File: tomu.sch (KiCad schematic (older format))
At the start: 15 parts, among them P1 USART0, P2 DEBUG, P3 USB-PCB, U1 EFM32HG309

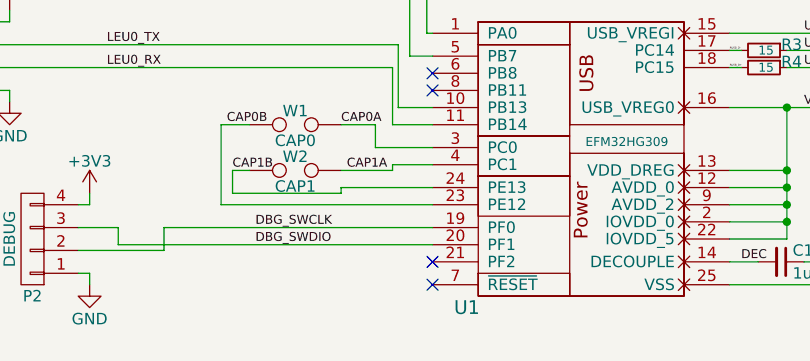
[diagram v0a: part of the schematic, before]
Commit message: Making pin 21 gnd.
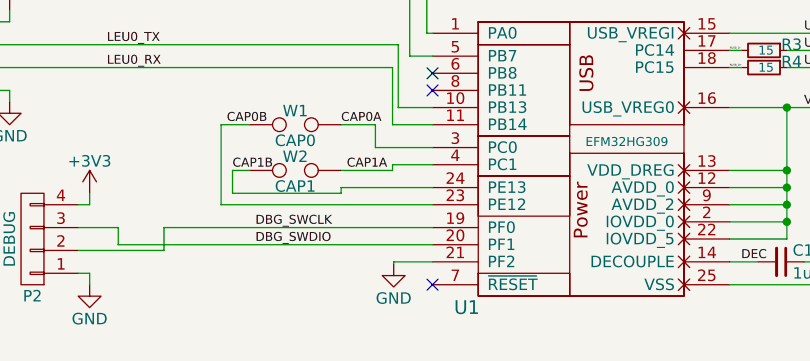
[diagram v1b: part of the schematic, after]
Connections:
- net GND: now also U1.21 (PF2)
- no-connect marks 4 -> 3
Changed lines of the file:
@@
 PB8 - US0_RX\nPB7 - US0_TX\n\nPA0 - Timer 0 Capture Compare Channel 0 -- For PWM - LED0 \nPB7 - Timer 1 Capture Compare Channel 0 -- For PWM - LED1\n\nPC0 - ACMP0_CH0 - Capacitive Touch 0\nPC1 - ACMP0_CH1 - Capacitive Touch 1\n\nPC14 - USB_DM\nPC15 - USB_DP\n\nPE12 - ADC0_CH0\nPE13 - ADC0_CH1\n\nPF0 - DBG_SWCLK #0 - BOOT_RX\nPF1 - DBG_SWDIO #0 - BOOT_TX\n\n
 NoConn ~ 4200 4125
-NoConn ~ 4200 4025
 Text Label 3800 3425 0    39   ~ 0
 CAP0A
@@
 NoConn ~ 4200 3200
 NoConn ~ 4200 3275
+$Comp
+L GND #PWR?
+U 1 1 57A1602A
+P 4030 4035
+F 0 "#PWR?" H 4030 3785 50  0001 C CNN
+F 1 "GND" H 4030 3885 50  0000 C CNN
+F 2 "" H 4030 4035 50  0000 C CNN
+F 3 "" H 4030 4035 50  0000 C CNN
+	1    4030 4035
+	1    0    0    -1
+$EndComp
+Wire Wire Line
+	4200 4025 4030 4025
+Wire Wire Line
+	4030 4025 4030 4035
 $EndSCHEMATC

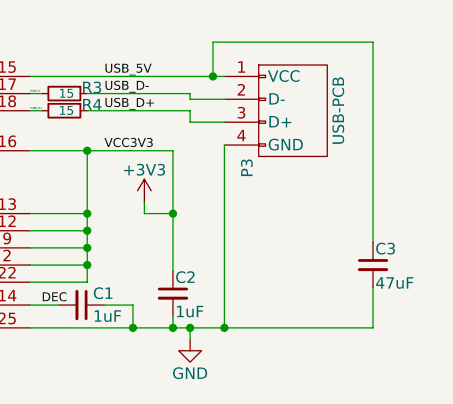
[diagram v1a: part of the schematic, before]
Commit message: 4.7uF not 47uF
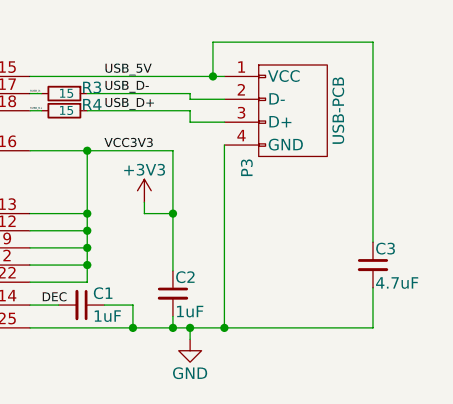
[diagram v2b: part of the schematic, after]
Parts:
- C3: value 47uF -> 4.7uF
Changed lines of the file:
@@
 P 7000 3850
 F 0 "C3" H 7010 3920 50  0000 L CNN
-F 1 "47uF" H 7010 3770 50  0000 L CNN
+F 1 "4.7uF" H 7010 3770 50  0000 L CNN
 F 2 "Capacitors_SMD:C_0402" H 7000 3850 50  0001 C CNN
 F 3 "" H 7000 3850 50  0000 C CNN

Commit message: v0.4: make board slimmer, increase tab size
Make the board slimmer, which will make plastics easier to fabricate.

Also make the tab size bigger, because that should be useful for
something.

Signed-off-by: Sean Cross <sean@xobs.io>
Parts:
- removed P2: DEBUG, Pin_Headers:Pin_Header_Angled_1x04, symbol CONN_01X04
- added P2: DEBUG, usb-pcb:pads-1x3, symbol Conn_01x03
- D1, D2: symbol LED -> LED-RESCUE-tomu
- W1, W2: symbol TEST -> TEST-RESCUE-tomu
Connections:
- net DBG_SWCLK: now also P2.2 (Pin_2)
- net DBG_SWDIO: now also P2.3 (Pin_3)
- net GND: now also P2.1 (Pin_1)
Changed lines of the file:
@@
 EESchema Schematic File Version 2
+LIBS:tomu-rescue
 LIBS:power
 LIBS:device
@@
 	0    1    1    0
 $EndComp
-$Comp
-L CONN_01X04 P2
-U 1 1 5798E965
-P 2450 3925
-F 0 "P2" H 2450 4175 50  0000 C CNN
-F 1 "DEBUG" V 2550 3925 50  0000 C CNN
-F 2 "Pin_Headers:Pin_Header_Angled_1x04" H 2450 3925 50  0001 C CNN
-F 3 "" H 2450 3925 50  0000 C CNN
-	1    2450 3925
-	-1   0    0    1
-$EndComp
 Text Label 3425 3875 0    39   ~ 0
 DBG_SWCLK
@@
 $EndComp
 $Comp
-L +3V3 #PWR04
-U 1 1 5798F04E
-P 2700 3725
-F 0 "#PWR04" H 2700 3575 50  0001 C CNN
-F 1 "+3V3" H 2700 3865 50  0000 C CNN
-F 2 "" H 2700 3725 50  0000 C CNN
-F 3 "" H 2700 3725 50  0000 C CNN
-	1    2700 3725
-	1    0    0    -1
-$EndComp
-$Comp
-L LED D1
+L LED-RESCUE-tomu D1
 U 1 1 5798F0D5
 P 3325 2425
@@
 $EndComp
 $Comp
-L LED D2
+L LED-RESCUE-tomu D2
 U 1 1 5798F173
 P 3550 2425
@@
 $EndComp
 $Comp
-L GND #PWR05
+L GND #PWR04
 U 1 1 5798FD6B
 P 2350 3325
-F 0 "#PWR05" H 2350 3075 50  0001 C CNN
+F 0 "#PWR04" H 2350 3075 50  0001 C CNN
 F 1 "GND" H 2350 3175 50  0000 C CNN
 F 2 "" H 2350 3325 50  0000 C CNN
@@
 $EndComp
 $Comp
-L +3V3 #PWR06
+L +3V3 #PWR05
 U 1 1 5798FD73
 P 2350 2925
-F 0 "#PWR06" H 2350 2775 50  0001 C CNN
+F 0 "#PWR05" H 2350 2775 50  0001 C CNN
 F 1 "+3V3" H 2350 3065 50  0000 C CNN
 F 2 "" H 2350 2925 50  0000 C CNN
@@
 $EndComp
 $Comp
-L TEST W1
+L TEST-RESCUE-tomu W1
 U 1 1 57990318
 P 3600 3425
@@
 $EndComp
 $Comp
-L TEST W2
+L TEST-RESCUE-tomu W2
 U 1 1 57990582
 P 3600 3625
@@
 CAP1B
 $Comp
-L +3V3 #PWR07
+L +3V3 #PWR06
 U 1 1 579B6568
 P 3450 2675
-F 0 "#PWR07" H 3450 2525 50  0001 C CNN
+F 0 "#PWR06" H 3450 2525 50  0001 C CNN
 F 1 "+3V3" H 3450 2815 50  0000 C CNN
 F 2 "" H 3450 2675 50  0000 C CNN
@@
 	2700 4075 2700 4125
 Wire Wire Line
-	2650 3775 2700 3775
-Wire Wire Line
-	2700 3775 2700 3725
-Wire Wire Line
 	6000 3575 6000 3625
 Wire Wire Line
@@
 NoConn ~ 4200 3275
 $Comp
-L GND #PWR?
+L GND #PWR07
 U 1 1 57A1602A
 P 4030 4035
-F 0 "#PWR?" H 4030 3785 50  0001 C CNN
+F 0 "#PWR07" H 4030 3785 50  0001 C CNN
 F 1 "GND" H 4030 3885 50  0000 C CNN
 F 2 "" H 4030 4035 50  0000 C CNN
@@
 Wire Wire Line
 	4030 4025 4030 4035
+$Comp
+L Conn_01x03 P2
+U 1 1 5A55837D
+P 2450 3975
+F 0 "P2" H 2450 4175 50  0000 C CNN
+F 1 "DEBUG" H 2450 3775 50  0000 C CNN
+F 2 "usb-pcb:pads-1x3" H 2450 3975 50  0001 C CNN
+F 3 "" H 2450 3975 50  0001 C CNN
+	1    2450 3975
+	-1   0    0    1
+$EndComp
+$Comp
+L PWR_FLAG #FLG08
+U 1 1 5A55865E
+P 6605 4125
+F 0 "#FLG08" H 6605 4200 50  0001 C CNN
+F 1 "PWR_FLAG" H 6605 4275 50  0000 C CNN
+F 2 "" H 6605 4125 50  0001 C CNN
+F 3 "" H 6605 4125 50  0001 C CNN
+	1    6605 4125
+	1    0    0    -1
+$EndComp
+Connection ~ 6605 4125
 $EndSCHEMATC

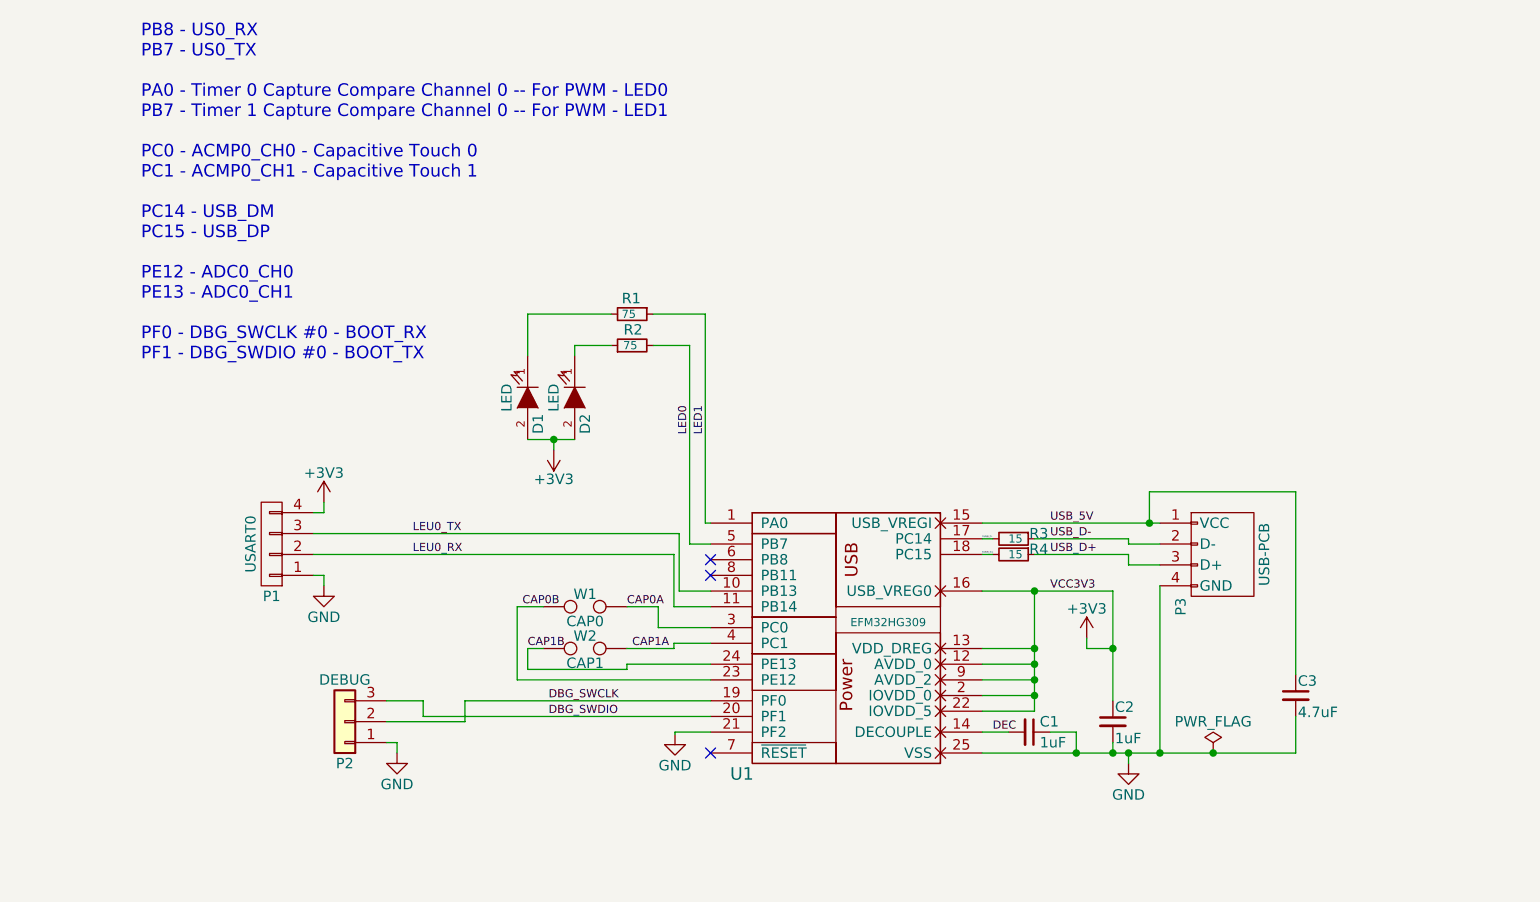
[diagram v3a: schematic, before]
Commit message: v0.4: rework board to be 1.0mm slimmer
Rework the main PCB to be slightly slimmer, a total of 10mm wide.  This
allows us to have 1mm of space on each side, which is enough for an
injection-molded case to be made.

Signed-off-by: Sean Cross <sean@xobs.io>
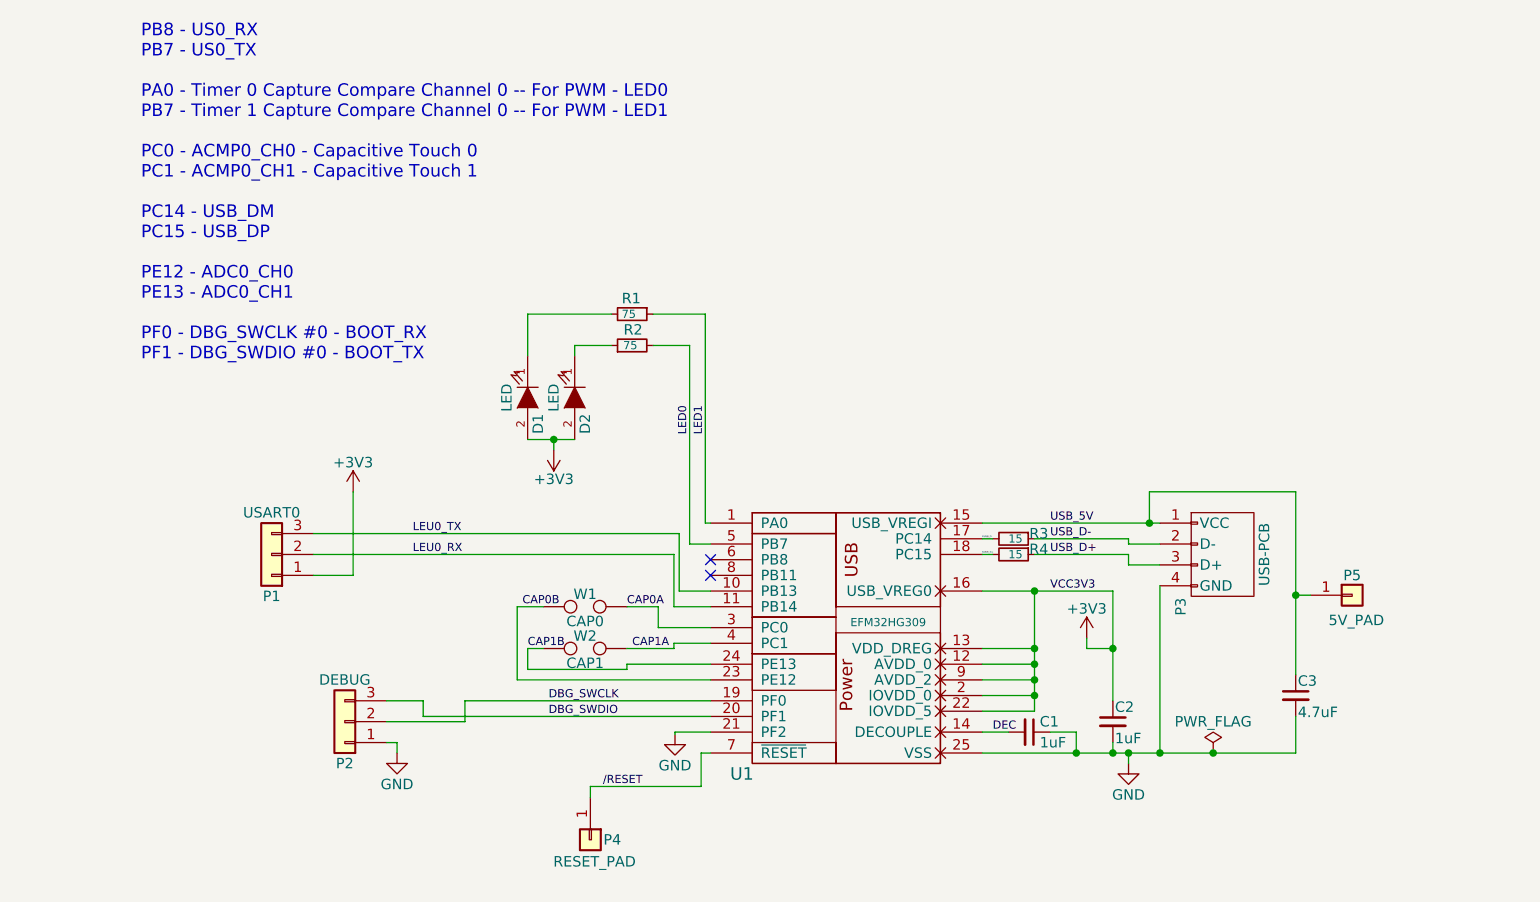
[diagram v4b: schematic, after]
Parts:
- removed P1: USART0, Pin_Headers:Pin_Header_Angled_1x04, symbol CONN_01X04
- added P1: USART0, usb-pcb:pads-1x3-slim, symbol Conn_01x03
- added P4: RESET_PAD, usb-pcb:pads-1x1, symbol Conn_01x01
- added P5: 5V_PAD, usb-pcb:pads-1x1, symbol Conn_01x01
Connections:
- net +3V3: now also P1.1 (Pin_1)
- net LEU0_RX: now also P1.2 (Pin_2)
- net LEU0_TX: now also P1.3 (Pin_3)
- net USB_5V: now also P5.1 (Pin_1)
- net /RESET: now reaches U1.7 (~RESET)
- net /RESET: now also P4.1 (Pin_1)
- no-connect marks 3 -> 2
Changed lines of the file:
@@
 $EndComp
 $Comp
-L CONN_01X04 P1
-U 1 1 5798FD61
-P 2100 3125
-F 0 "P1" H 2100 3375 50  0000 C CNN
-F 1 "USART0" V 2200 3125 50  0000 C CNN
-F 2 "Pin_Headers:Pin_Header_Angled_1x04" H 2100 3125 50  0001 C CNN
-F 3 "" H 2100 3125 50  0000 C CNN
-	1    2100 3125
-	-1   0    0    1
-$EndComp
-$Comp
-L GND #PWR04
-U 1 1 5798FD6B
-P 2350 3325
-F 0 "#PWR04" H 2350 3075 50  0001 C CNN
-F 1 "GND" H 2350 3175 50  0000 C CNN
-F 2 "" H 2350 3325 50  0000 C CNN
-F 3 "" H 2350 3325 50  0000 C CNN
-	1    2350 3325
-	1    0    0    -1
-$EndComp
-$Comp
-L +3V3 #PWR05
+L +3V3 #PWR04
 U 1 1 5798FD73
-P 2350 2925
-F 0 "#PWR05" H 2350 2775 50  0001 C CNN
-F 1 "+3V3" H 2350 3065 50  0000 C CNN
-F 2 "" H 2350 2925 50  0000 C CNN
-F 3 "" H 2350 2925 50  0000 C CNN
-	1    2350 2925
+P 2490 2875
+F 0 "#PWR04" H 2490 2725 50  0001 C CNN
+F 1 "+3V3" H 2490 3015 50  0000 C CNN
+F 2 "" H 2490 2875 50  0000 C CNN
+F 3 "" H 2490 2875 50  0000 C CNN
+	1    2490 2875
 	1    0    0    -1
 $EndComp
@@
 Text Notes 1475 2350 0    60   ~ 0
 PB8 - US0_RX\nPB7 - US0_TX\n\nPA0 - Timer 0 Capture Compare Channel 0 -- For PWM - LED0 \nPB7 - Timer 1 Capture Compare Channel 0 -- For PWM - LED1\n\nPC0 - ACMP0_CH0 - Capacitive Touch 0\nPC1 - ACMP0_CH1 - Capacitive Touch 1\n\nPC14 - USB_DM\nPC15 - USB_DP\n\nPE12 - ADC0_CH0\nPE13 - ADC0_CH1\n\nPF0 - DBG_SWCLK #0 - BOOT_RX\nPF1 - DBG_SWDIO #0 - BOOT_TX\n\n
-NoConn ~ 4200 4125
 Text Label 3800 3425 0    39   ~ 0
 CAP0A
@@
 CAP1B
 $Comp
-L +3V3 #PWR06
+L +3V3 #PWR05
 U 1 1 579B6568
 P 3450 2675
-F 0 "#PWR06" H 3450 2525 50  0001 C CNN
+F 0 "#PWR05" H 3450 2525 50  0001 C CNN
 F 1 "+3V3" H 3450 2815 50  0000 C CNN
 F 2 "" H 3450 2675 50  0000 C CNN
@@
 	1    0    0    -1
 $EndComp
-Wire Wire Line
-	5500 3350 6125 3350
-Wire Wire Line
-	5750 3625 5500 3625
-Connection ~ 5750 3350
-Connection ~ 5750 3625
-Wire Wire Line
-	6200 4125 6200 4175
-Wire Wire Line
-	6125 4125 6125 4075
-Connection ~ 6200 4125
-Wire Wire Line
-	5950 4025 5950 4125
-Connection ~ 6125 4125
-Wire Wire Line
-	6125 3350 6125 3875
-Wire Wire Line
-	5750 3350 5750 3925
-Wire Wire Line
-	5550 3100 5500 3100
-Wire Wire Line
-	5500 3175 5550 3175
-Wire Wire Line
-	5500 3025 6350 3025
-Wire Wire Line
-	5750 3100 6200 3100
-Wire Wire Line
-	6350 3125 6200 3125
-Wire Wire Line
-	6200 3125 6200 3100
-Wire Wire Line
-	6350 3225 6200 3225
-Wire Wire Line
-	6200 3225 6200 3175
-Wire Wire Line
-	6200 3175 5750 3175
-Wire Wire Line
-	5500 4125 7000 4125
-Wire Wire Line
-	7000 4125 7000 3950
-Wire Wire Line
-	7000 3750 7000 2875
-Wire Wire Line
-	7000 2875 6300 2875
-Wire Wire Line
-	6300 2875 6300 3025
-Connection ~ 6300 3025
-Wire Wire Line
-	5750 3700 5500 3700
-Wire Wire Line
-	5750 3775 5500 3775
-Connection ~ 5750 3700
-Wire Wire Line
-	5750 3850 5500 3850
-Connection ~ 5750 3775
-Wire Wire Line
-	5750 3925 5500 3925
-Connection ~ 5750 3850
-Wire Wire Line
-	5500 4025 5625 4025
-Wire Wire Line
-	5825 4025 5950 4025
-Connection ~ 5950 4125
-Wire Wire Line
-	3025 3875 4200 3875
-Wire Wire Line
-	2825 3950 4200 3950
-Wire Wire Line
-	2650 4075 2700 4075
-Wire Wire Line
-	2700 4075 2700 4125
-Wire Wire Line
-	6000 3575 6000 3625
-Wire Wire Line
-	6000 3625 6125 3625
-Connection ~ 6125 3625
-Wire Wire Line
-	6350 3325 6350 4125
-Connection ~ 6350 4125
-Wire Wire Line
-	3450 2675 3450 2625
-Wire Wire Line
-	3325 2625 3550 2625
-Connection ~ 3450 2625
-Wire Wire Line
-	3725 2175 3550 2175
-Wire Wire Line
-	3550 2175 3550 2225
-Wire Wire Line
-	3725 2025 3325 2025
-Wire Wire Line
-	3325 2025 3325 2225
-Wire Wire Line
-	2300 3275 2350 3275
-Wire Wire Line
-	2350 3275 2350 3325
-Wire Wire Line
-	2300 2975 2350 2975
-Wire Wire Line
-	2350 2975 2350 2925
-Wire Wire Line
-	4175 2025 4175 3025
-Wire Wire Line
-	3325 3625 3400 3625
-Wire Wire Line
-	3275 3425 3400 3425
-Wire Wire Line
-	3800 3425 3950 3425
-Wire Wire Line
-	3950 3425 3950 3525
-Wire Wire Line
-	3950 3525 4200 3525
-Wire Wire Line
-	4200 3600 4025 3600
-Wire Wire Line
-	4025 3625 3800 3625
-Wire Wire Line
-	4175 2025 3925 2025
-Wire Wire Line
-	2300 3075 4050 3075
-Wire Wire Line
-	2300 3175 4025 3175
-Wire Wire Line
-	4100 3125 4100 2175
-Wire Wire Line
-	4100 2175 3925 2175
-Wire Wire Line
-	3800 3700 4200 3700
-Wire Wire Line
-	3275 3775 4200 3775
-Wire Wire Line
-	4025 3600 4025 3625
-Wire Wire Line
-	3800 3700 3800 3725
-Wire Wire Line
-	3800 3725 3325 3725
-Wire Wire Line
-	3325 3725 3325 3625
-Wire Wire Line
-	3275 3775 3275 3425
-Wire Wire Line
-	2825 3950 2825 3875
-Wire Wire Line
-	2825 3875 2650 3875
-Wire Wire Line
-	3025 3875 3025 3975
-Wire Wire Line
-	3025 3975 2650 3975
-Wire Wire Line
-	4200 3350 4050 3350
-Wire Wire Line
-	4050 3350 4050 3075
-Wire Wire Line
-	4200 3425 4025 3425
-Wire Wire Line
-	4025 3425 4025 3175
-Wire Wire Line
-	4175 3025 4200 3025
-Wire Wire Line
-	4100 3125 4200 3125
 NoConn ~ 4200 3200
 NoConn ~ 4200 3275
 $Comp
-L GND #PWR07
+L GND #PWR06
 U 1 1 57A1602A
 P 4030 4035
-F 0 "#PWR07" H 4030 3785 50  0001 C CNN
+F 0 "#PWR06" H 4030 3785 50  0001 C CNN
 F 1 "GND" H 4030 3885 50  0000 C CNN
 F 2 "" H 4030 4035 50  0000 C CNN
@@
 	1    0    0    -1
 $EndComp
-Wire Wire Line
-	4200 4025 4030 4025
-Wire Wire Line
-	4030 4025 4030 4035
 $Comp
 L Conn_01x03 P2
@@
 $EndComp
 $Comp
-L PWR_FLAG #FLG08
+L PWR_FLAG #FLG07
 U 1 1 5A55865E
 P 6605 4125
-F 0 "#FLG08" H 6605 4200 50  0001 C CNN
+F 0 "#FLG07" H 6605 4200 50  0001 C CNN
 F 1 "PWR_FLAG" H 6605 4275 50  0000 C CNN
 F 2 "" H 6605 4125 50  0001 C CNN
@@
 	1    0    0    -1
 $EndComp
+Wire Wire Line
+	5500 3350 6125 3350
+Wire Wire Line
+	5750 3625 5500 3625
+Connection ~ 5750 3350
+Connection ~ 5750 3625
+Wire Wire Line
+	6200 4125 6200 4175
+Wire Wire Line
+	6125 4125 6125 4075
+Connection ~ 6200 4125
+Wire Wire Line
+	5950 4025 5950 4125
+Connection ~ 6125 4125
+Wire Wire Line
+	6125 3350 6125 3875
+Wire Wire Line
+	5750 3350 5750 3925
+Wire Wire Line
+	5550 3100 5500 3100
+Wire Wire Line
+	5500 3175 5550 3175
+Wire Wire Line
+	5500 3025 6350 3025
+Wire Wire Line
+	5750 3100 6200 3100
+Wire Wire Line
+	6350 3125 6200 3125
+Wire Wire Line
+	6200 3125 6200 3100
+Wire Wire Line
+	6350 3225 6200 3225
+Wire Wire Line
+	6200 3225 6200 3175
+Wire Wire Line
+	6200 3175 5750 3175
+Wire Wire Line
+	5500 4125 7000 4125
+Wire Wire Line
+	7000 4125 7000 3950
+Wire Wire Line
+	7000 3750 7000 2875
+Wire Wire Line
+	7000 2875 6300 2875
+Wire Wire Line
+	6300 2875 6300 3025
+Connection ~ 6300 3025
+Wire Wire Line
+	5750 3700 5500 3700
+Wire Wire Line
+	5750 3775 5500 3775
+Connection ~ 5750 3700
+Wire Wire Line
+	5750 3850 5500 3850
+Connection ~ 5750 3775
+Wire Wire Line
+	5750 3925 5500 3925
+Connection ~ 5750 3850
+Wire Wire Line
+	5500 4025 5625 4025
+Wire Wire Line
+	5825 4025 5950 4025
+Connection ~ 5950 4125
+Wire Wire Line
+	3025 3875 4200 3875
+Wire Wire Line
+	2825 3950 4200 3950
+Wire Wire Line
+	2650 4075 2700 4075
+Wire Wire Line
+	2700 4075 2700 4125
+Wire Wire Line
+	6000 3575 6000 3625
+Wire Wire Line
+	6000 3625 6125 3625
+Connection ~ 6125 3625
+Wire Wire Line
+	6350 3325 6350 4125
+Connection ~ 6350 4125
+Wire Wire Line
+	3450 2675 3450 2625
+Wire Wire Line
+	3325 2625 3550 2625
+Connection ~ 3450 2625
+Wire Wire Line
+	3725 2175 3550 2175
+Wire Wire Line
+	3550 2175 3550 2225
+Wire Wire Line
+	3725 2025 3325 2025
+Wire Wire Line
+	3325 2025 3325 2225
+Wire Wire Line
+	4175 2025 4175 3025
+Wire Wire Line
+	3325 3625 3400 3625
+Wire Wire Line
+	3275 3425 3400 3425
+Wire Wire Line
+	3800 3425 3950 3425
+Wire Wire Line
+	3950 3425 3950 3525
+Wire Wire Line
+	3950 3525 4200 3525
+Wire Wire Line
+	4200 3600 4025 3600
+Wire Wire Line
+	4025 3625 3800 3625
+Wire Wire Line
+	4175 2025 3925 2025
+Wire Wire Line
+	2300 3075 4050 3075
+Wire Wire Line
+	2300 3175 4025 3175
+Wire Wire Line
+	4100 3125 4100 2175
+Wire Wire Line
+	4100 2175 3925 2175
+Wire Wire Line
+	3800 3700 4200 3700
+Wire Wire Line
+	3275 3775 4200 3775
+Wire Wire Line
+	4025 3600 4025 3625
+Wire Wire Line
+	3800 3700 3800 3725
+Wire Wire Line
+	3800 3725 3325 3725
+Wire Wire Line
+	3325 3725 3325 3625
+Wire Wire Line
+	3275 3775 3275 3425
+Wire Wire Line
+	2825 3950 2825 3875
+Wire Wire Line
+	2825 3875 2650 3875
+Wire Wire Line
+	3025 3875 3025 3975
+Wire Wire Line
+	3025 3975 2650 3975
+Wire Wire Line
+	4200 3350 4050 3350
+Wire Wire Line
+	4050 3350 4050 3075
+Wire Wire Line
+	4200 3425 4025 3425
+Wire Wire Line
+	4025 3425 4025 3175
+Wire Wire Line
+	4175 3025 4200 3025
+Wire Wire Line
+	4100 3125 4200 3125
+Wire Wire Line
+	4200 4025 4030 4025
+Wire Wire Line
+	4030 4025 4030 4035
 Connection ~ 6605 4125
+Wire Wire Line
+	2300 3275 2490 3275
+Wire Wire Line
+	2490 3275 2490 2875
+Wire Wire Line
+	4200 4125 4155 4125
+Wire Wire Line
+	4155 4125 4155 4285
+Text Label 3685 4285 0    39   ~ 0
+/RESET
+$Comp
+L Conn_01x03 P1
+U 1 1 5A55AC38
+P 2100 3175
+F 0 "P1" H 2100 3375 50  0000 C CNN
+F 1 "USART0" H 2100 2975 50  0000 C CNN
+F 2 "usb-pcb:pads-1x3-slim" H 2100 3175 50  0001 C CNN
+F 3 "" H 2100 3175 50  0001 C CNN
+	1    2100 3175
+	-1   0    0    1
+$EndComp
+Wire Wire Line
+	4155 4285 3625 4285
+Wire Wire Line
+	3625 4285 3625 4340
+$Comp
+L Conn_01x01 P4
+U 1 1 5A55B1FF
+P 3625 4540
+F 0 "P4" V 3625 4645 50  0000 C CNN
+F 1 "RESET_PAD" V 3730 4560 50  0000 C CNN
+F 2 "usb-pcb:pads-1x1" H 3625 4540 50  0001 C CNN
+F 3 "" H 3625 4540 50  0001 C CNN
+	1    3625 4540
+	0    1    1    0
+$EndComp
+$Comp
+L Conn_01x01 P5
+U 1 1 5A55B8D8
+P 7270 3370
+F 0 "P5" H 7270 3465 50  0000 C CNN
+F 1 "5V_PAD" H 7290 3250 50  0000 C CNN
+F 2 "usb-pcb:pads-1x1" H 7270 3370 50  0001 C CNN
+F 3 "" H 7270 3370 50  0001 C CNN
+	1    7270 3370
+	1    0    0    -1
+$EndComp
+Wire Wire Line
+	7070 3370 7000 3370
+Connection ~ 7000 3370
 $EndSCHEMATC
